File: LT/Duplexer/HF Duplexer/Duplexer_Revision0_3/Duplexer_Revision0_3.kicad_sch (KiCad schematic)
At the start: 34 parts, among them J1 SMA_CONNECTOR, J2 SMA_CONNECTOR, J3 SMA_CONNECTOR, J4 SMA_CONNECTOR

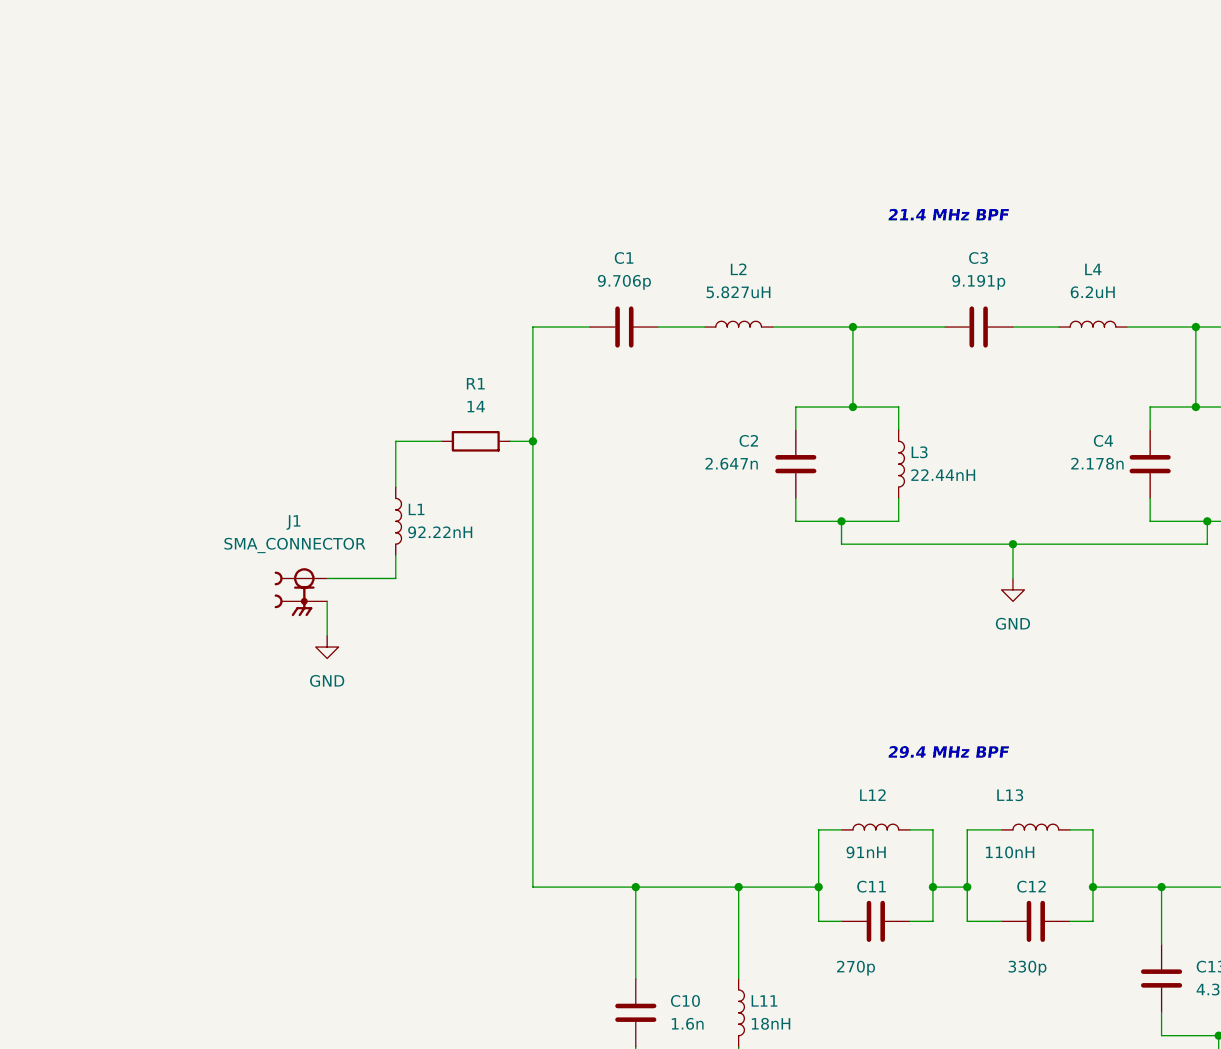
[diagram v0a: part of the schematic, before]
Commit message: I added some variable caps and inductors to the Duplexer Rev0.3 will add more soon
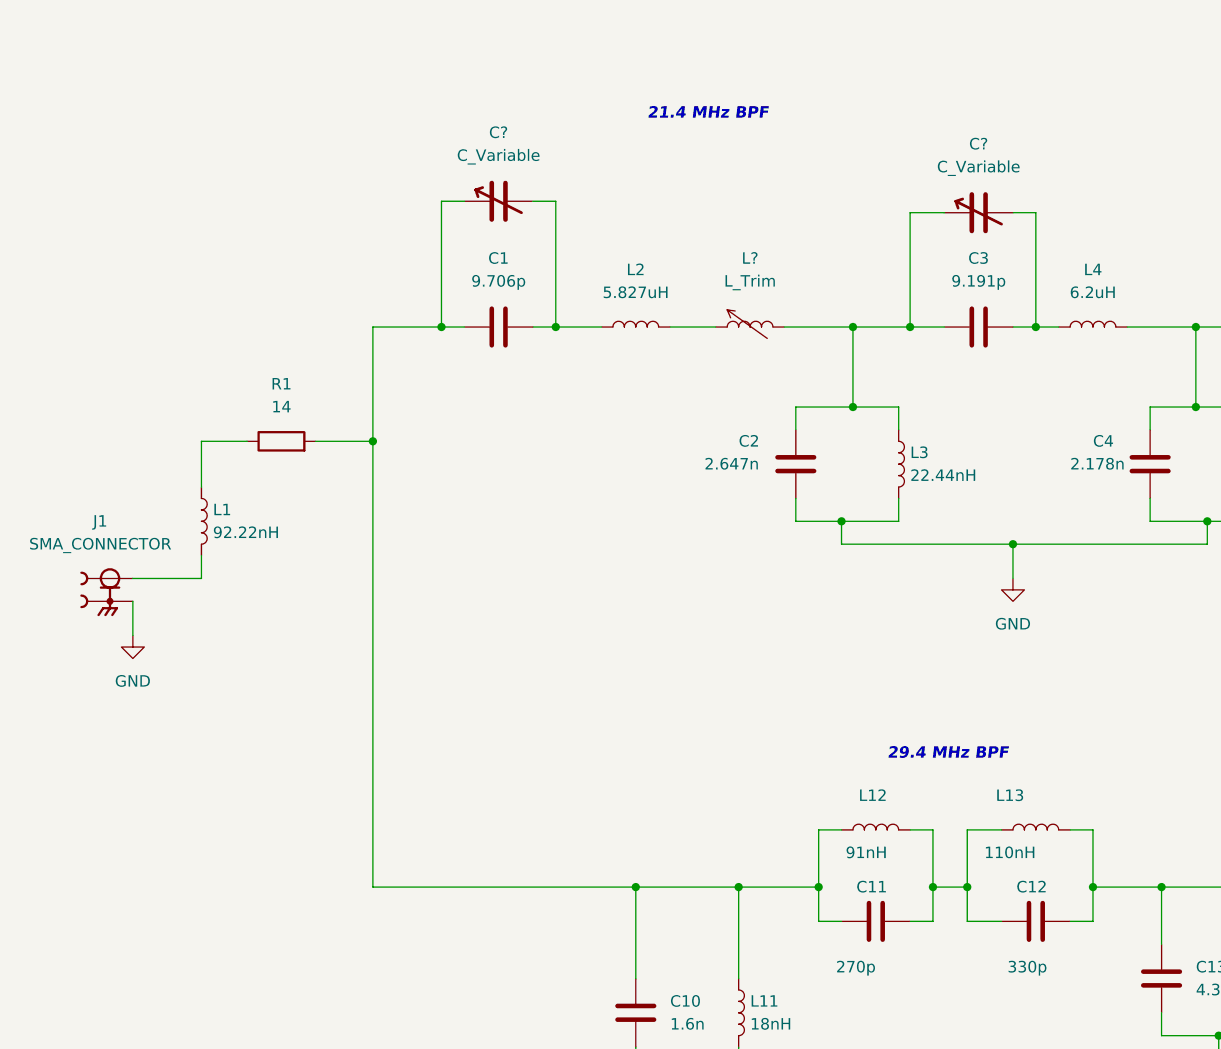
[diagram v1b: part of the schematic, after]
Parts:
- added C? (x2): C_Variable, symbol Device:C_Variable
- added L?: L_Trim, symbol Device:L_Trim
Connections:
- net at C1.2, L2.1: now also C?.2
- net at C2.2, C3.1, L3.1: now also C?.1, L?.2; no longer L2.2
- net at C1.1, C10.1, C11.1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: now also C?.1
- net at C3.2, L4.1: now also C?.2
- new net: L2.2, L?.1
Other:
- moved on the sheet: C1, J1, L1, L2, R1

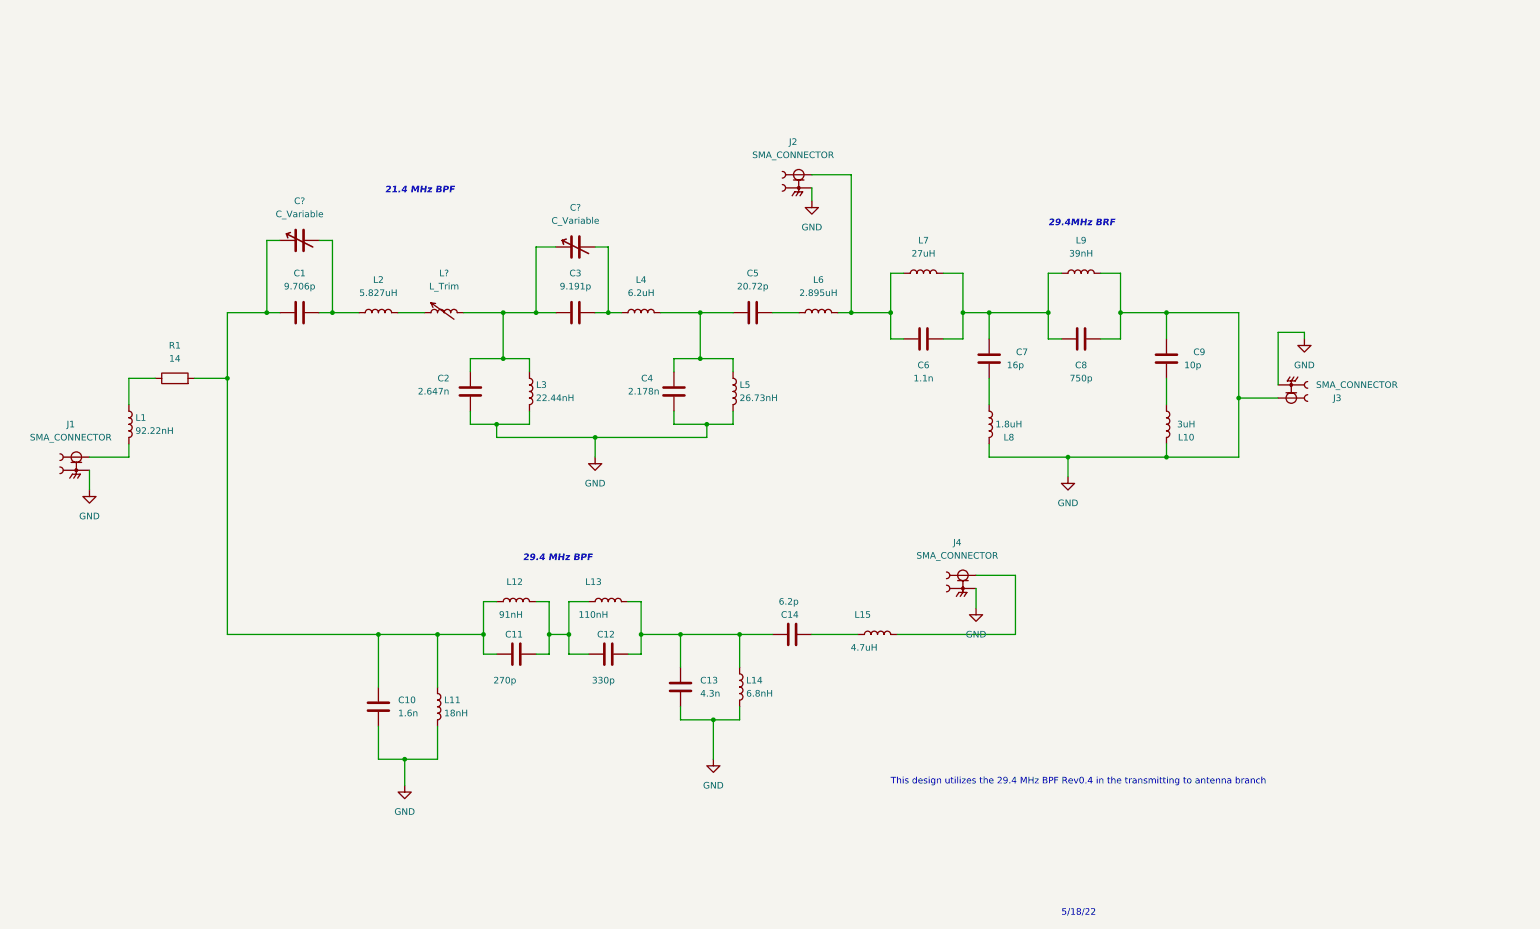
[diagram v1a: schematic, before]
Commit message: I added more variable caps and inductors to the Duplexer Rev0.3 KiCad design
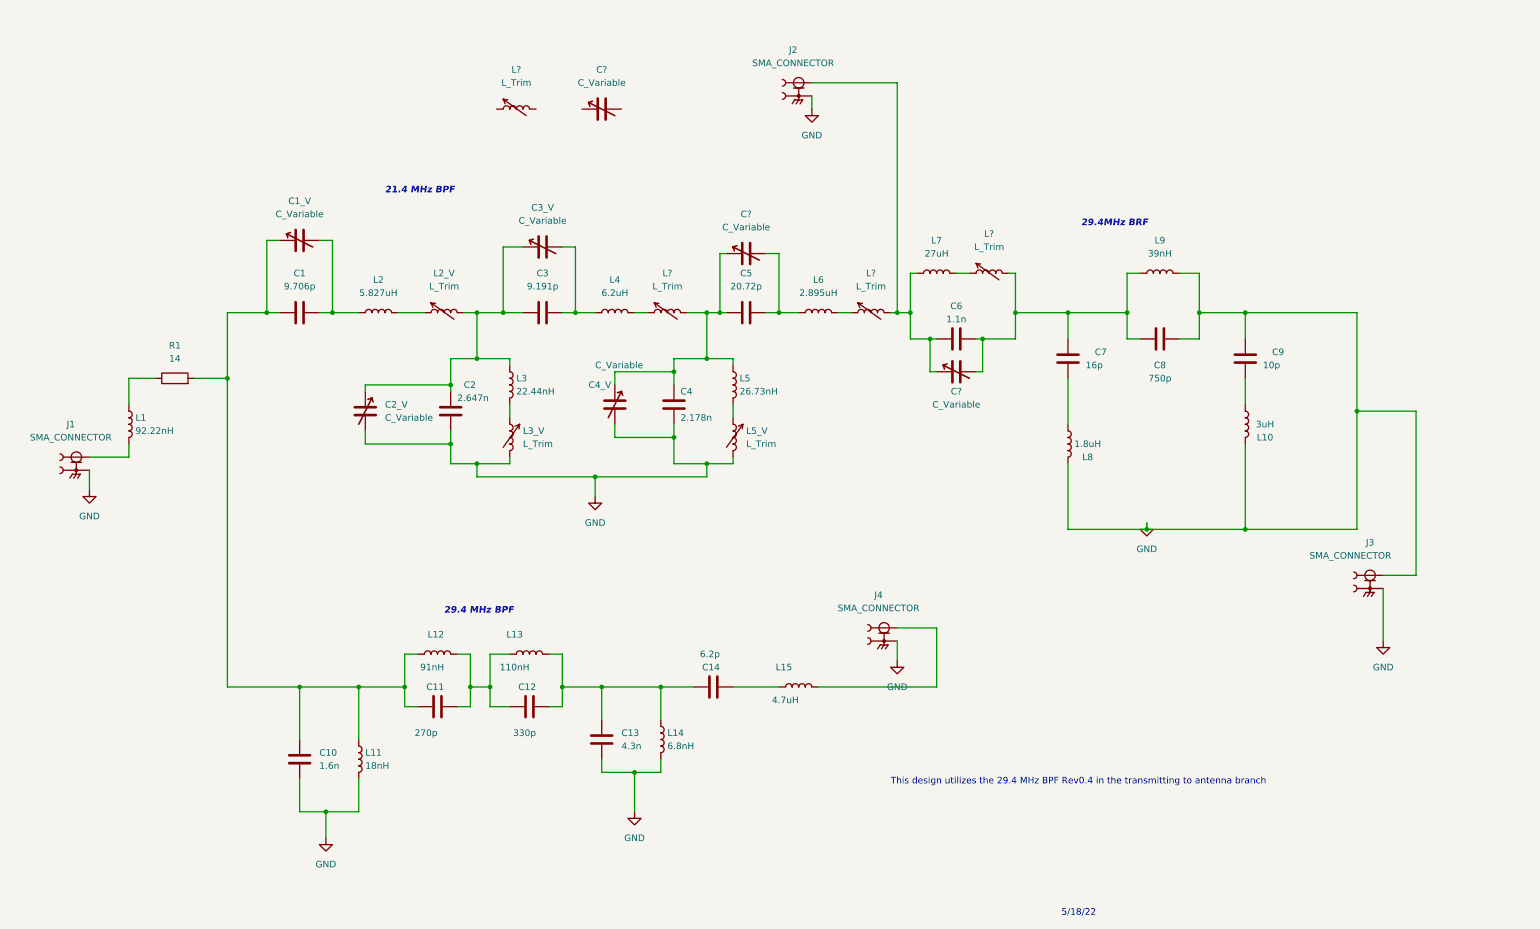
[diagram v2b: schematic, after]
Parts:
- added C2_V, C4_V, C? (x3): C_Variable, symbol Device:C_Variable
- added L3_V, L5_V, L? (x4): L_Trim, symbol Device:L_Trim
- gave numbers to parts that had none: 3
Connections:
- net GND: now also C2_V.2, C4_V.2, L3_V.2, L5_V.2; no longer L3.2, L5.2
- net at C2.2, C3.1, C3_V.1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: now also C2_V.1
- net at C5.2, L6.1: now also C?.2
- net at C6.2, J2.1, L7.1: now also C?.1, L?.2; no longer L6.2
- net at C6.1, C7.1, C8.2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: now also C?.2, L?.2; no longer L7.2
- net at C4.2, C5.1, L5.1: now also C4_V.1, C?.1, L?.2; no longer L4.2
- new net: L4.2, L?.1
- new net: L3.2, L3_V.1
- new net: L6.2, L?.1
- new net: L5.2, L5_V.1
- new net: L7.2, L?.1
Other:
- moved on the sheet: C10, C11, C12, C13, C14, C2, C3, C3_V, C4, C5, C6, C7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

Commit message: I added variable capacitors and inductors to the design
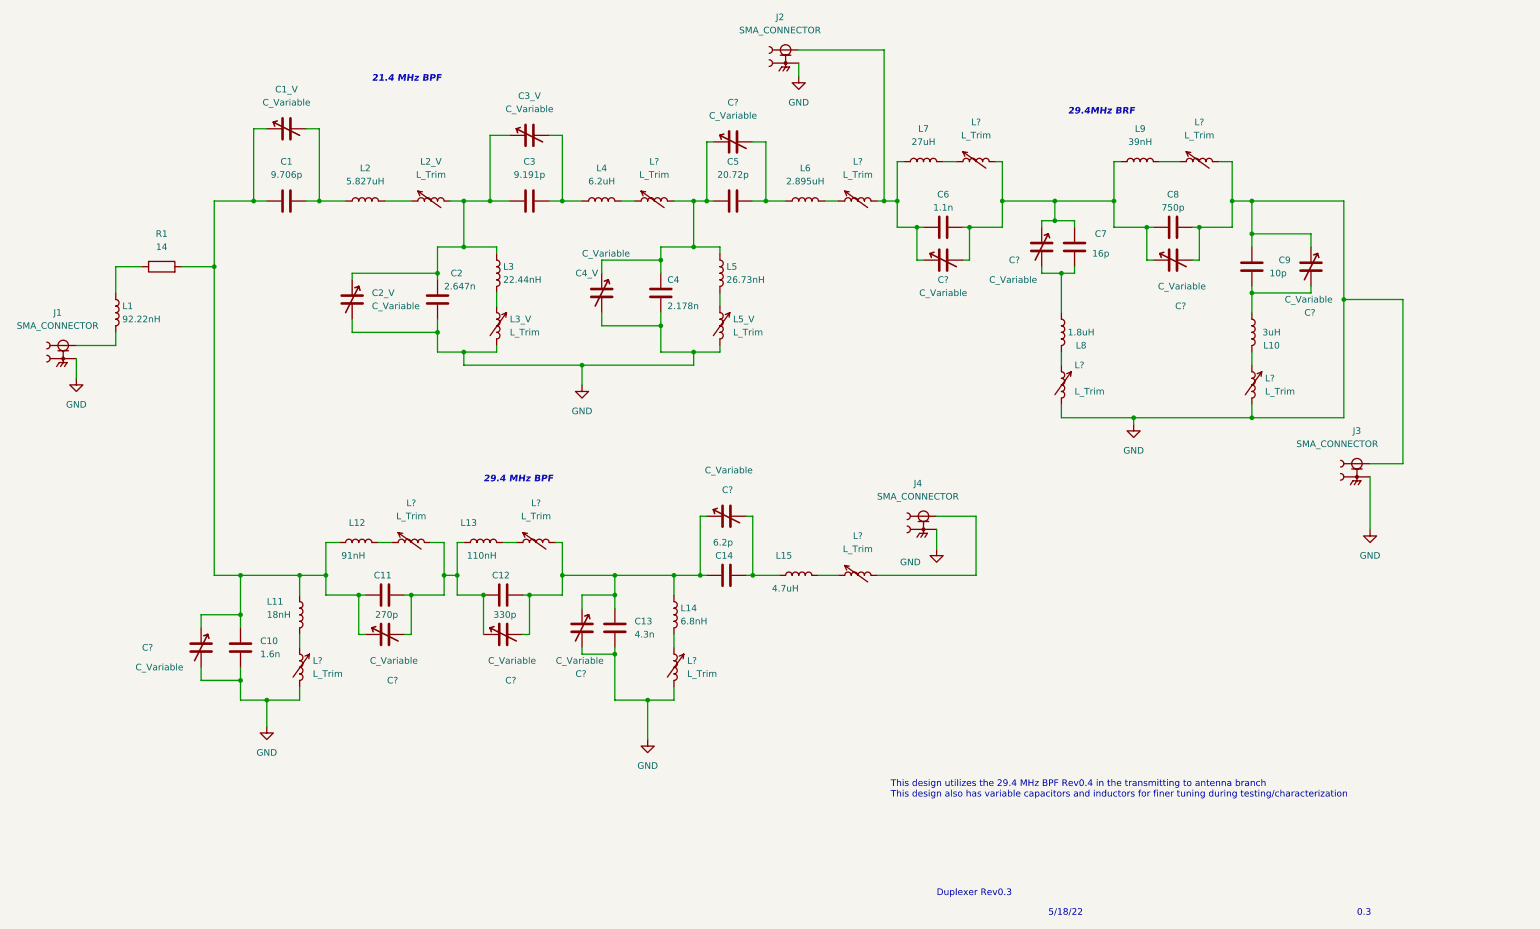
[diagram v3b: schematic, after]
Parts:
- removed C?: C_Variable, symbol Device:C_Variable
- removed L?: L_Trim, symbol Device:L_Trim
- added C? (x8): C_Variable, symbol Device:C_Variable
- added L? (x8): L_Trim, symbol Device:L_Trim
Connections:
- net GND: now also C?.1, C?.2, C?.2, C?.2, L?.2, L?.2, L?.2, L?.2, L?.2; no longer L10.2, L11.2, L14.2, L8.2, L9.2
- net at C7.2, L8.1: now also C?.2
- net at C14.2, L15.1: now also C?.2
- net at L15.2: now also L?.1; no longer J4.1
- net at C11.2, C12.1, L13.1: now also C?.1, C?.2, L?.2; no longer L12.2
- net at C12.2, C13.1, C14.1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: now also C?.1, C?.1, C?.2, L?.2; no longer L13.2
- net at C1.1, C10.1, C11.1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: now also C?.1, C?.1
- net at C6.1, C7.1, C8.2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: now also C?.1, C?.1
- net at C9.2, L10.1: now also C?.2
- new net: L8.2, L?.1
- new net: L10.2, L?.1
- new net: J4.1, L?.2
- new net: L9.2, L?.1
- new net: L13.2, L?.1
- new net: L12.2, L?.1
- new net: L11.2, L?.1
- new net: L14.2, L?.1
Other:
- note added: "0.3"
- note added: "Duplexer Rev0.3"
- note added: "This design utilizes the 29.4 MHz BPF Rev0.4 in the transmitting to antenna branch This design also has variable capacitors and inductors for finer tuning during testing/characterization"
- note removed: "This design utilizes the 29.4 MHz BPF Rev0.4 in the transmitting to antenna branch"
- moved on the sheet: C1, C10, C11, C12, C13, C14, C1_V, C2, C2_V, C3, C3_V, C4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

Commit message: I begin working on my duplexer rev0.31 in KiCad, I also added the needed footprints and symbols to the github
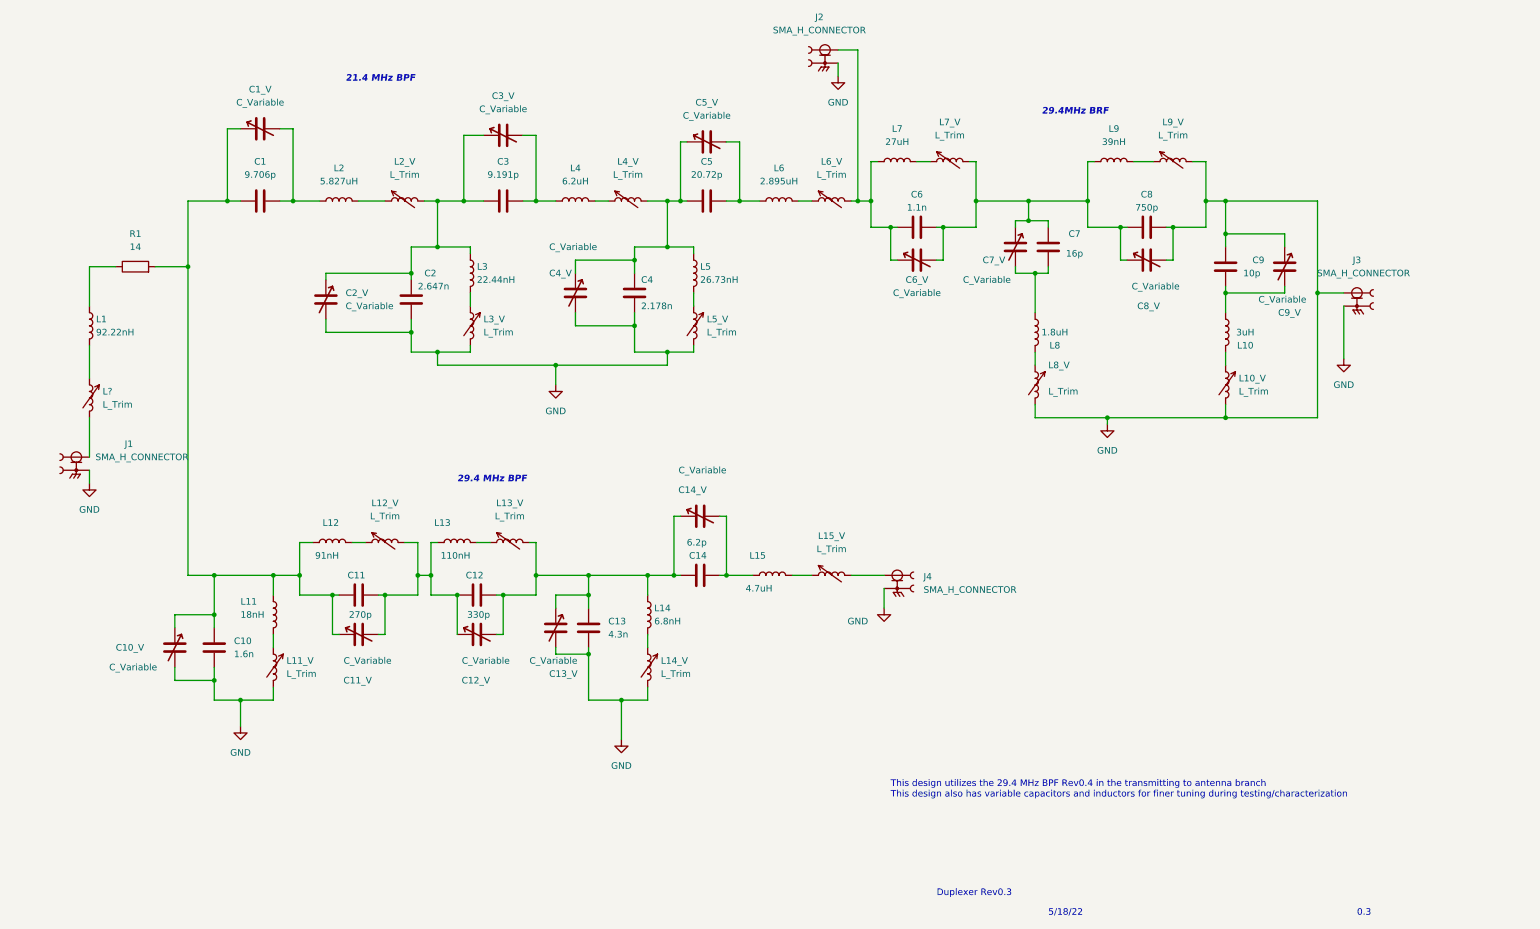
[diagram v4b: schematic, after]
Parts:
- added L?: L_Trim, symbol Device:L_Trim
- J1, J2, J3, J4: value SMA_CONNECTOR -> SMA_H_CONNECTOR
- gave numbers to parts that had none: 21
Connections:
- net at J1.1: now also L?.2; no longer L1.2
- new net: L1.2, L?.1
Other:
- moved on the sheet: C1, C10, C10_V, C11, C11_V, C12, C12_V, C13, C13_V, C14, C14_V, C1_V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
